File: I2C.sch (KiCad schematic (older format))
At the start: 1 part

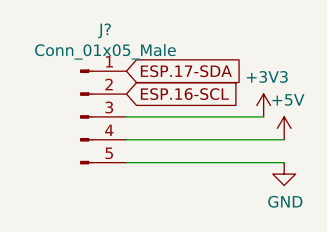
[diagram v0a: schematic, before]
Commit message: added sensors, finished schematics yet
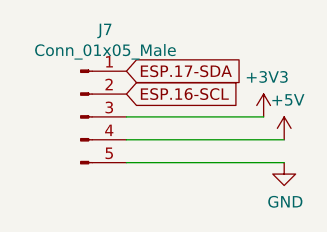
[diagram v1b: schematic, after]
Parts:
- J7: renamed from J?; footprint (none) -> Connector_PinHeader_2.54mm:PinHeader_1x05_P2.54mm_Vertical
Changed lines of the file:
@@
 $Descr A4 11693 8268
 encoding utf-8
-Sheet 12 13
+Sheet 12 14
 Title ""
 Date ""
@@
 ESP.17-SDA
 $Comp
-L Connector:Conn_01x05_Male J?
+L Connector:Conn_01x05_Male J7
 U 1 1 60D3C24A
 P 5000 3750
-F 0 "J?" H 5108 4131 50  0000 C CNN
+F 0 "J7" H 5108 4131 50  0000 C CNN
 F 1 "Conn_01x05_Male" H 5108 4040 50  0000 C CNN
-F 2 "" H 5000 3750 50  0001 C CNN
+F 2 "Connector_PinHeader_2.54mm:PinHeader_1x05_P2.54mm_Vertical" H 5000 3750 50  0001 C CNN
 F 3 "~" H 5000 3750 50  0001 C CNN
 	1    5000 3750
@@
 $EndComp
 $Comp
-L power:GND #PWR?
+L power:GND #PWR0126
 U 1 1 60D3B336
 P 5890 3950
-F 0 "#PWR?" H 5890 3700 50  0001 C CNN
+F 0 "#PWR0126" H 5890 3700 50  0001 C CNN
 F 1 "GND" H 5895 3777 50  0000 C CNN
 F 2 "" H 5890 3950 50  0001 C CNN
@@
 $EndComp
 $Comp
-L power:+5V #PWR?
+L power:+5V #PWR0127
 U 1 1 60D3ABC9
 P 5890 3850
-F 0 "#PWR?" H 5890 3700 50  0001 C CNN
+F 0 "#PWR0127" H 5890 3700 50  0001 C CNN
 F 1 "+5V" H 5905 4023 50  0000 C CNN
 F 2 "" H 5890 3850 50  0001 C CNN
@@
 $EndComp
 $Comp
-L power:+3V3 #PWR?
+L power:+3V3 #PWR0128
 U 1 1 60D40F25
 P 5800 3750
-F 0 "#PWR?" H 5800 3600 50  0001 C CNN
+F 0 "#PWR0128" H 5800 3600 50  0001 C CNN
 F 1 "+3V3" H 5815 3923 50  0000 C CNN
 F 2 "" H 5800 3750 50  0001 C CNN

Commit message: finished pcb layout. check needed.
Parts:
- J7: footprint Connector_PinHeader_2.54mm:PinHeader_1x05_P2.54mm_Vertical -> TerminalBlock:ScrewTerminal_1x5_P5.00
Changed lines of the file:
@@
 F 0 "J7" H 5108 4131 50  0000 C CNN
 F 1 "Conn_01x05_Male" H 5108 4040 50  0000 C CNN
-F 2 "Connector_PinHeader_2.54mm:PinHeader_1x05_P2.54mm_Vertical" H 5000 3750 50  0001 C CNN
+F 2 "TerminalBlock:ScrewTerminal_1x5_P5.00" H 5000 3750 50  0001 C CNN
 F 3 "~" H 5000 3750 50  0001 C CNN
 	1    5000 3750
